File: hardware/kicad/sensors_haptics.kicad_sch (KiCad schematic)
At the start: 9 parts, among them J9 LRA motor, U10 VEML7700-TT, U11 DRV2605LDGSR

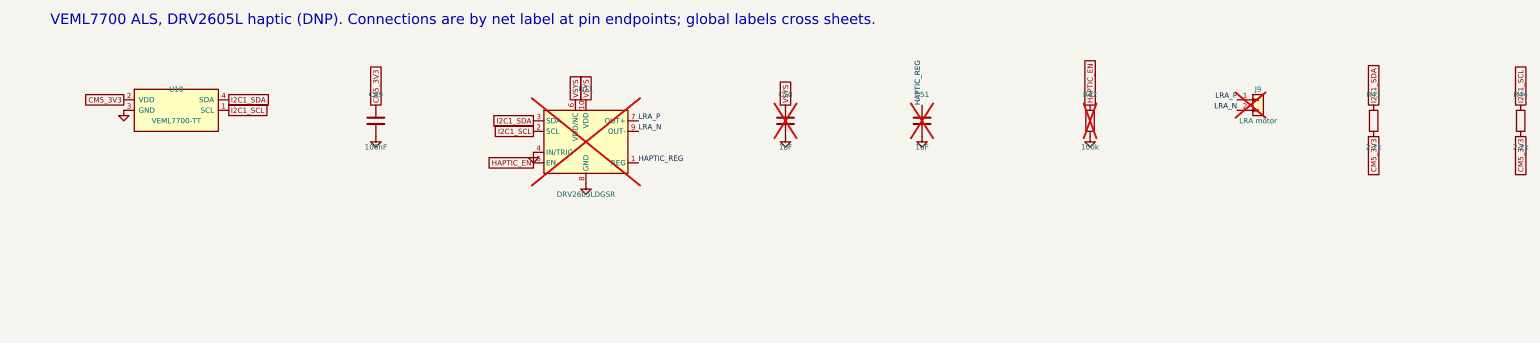
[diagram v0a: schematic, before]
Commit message: Sync KiCad schematic to netlist v3.2; add side_flex sheet
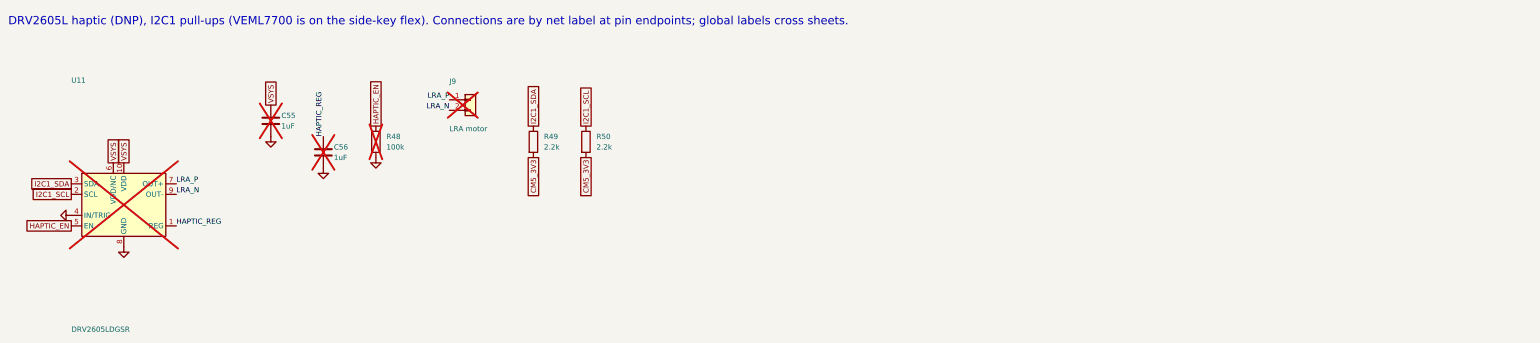
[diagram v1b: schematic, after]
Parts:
- removed C49: 100nF, Capacitor_SMD:C_0402_1005Metric, symbol Device:C
- removed C50, C51: 1uF, Capacitor_SMD:C_0402_1005Metric, symbol Device:C
- removed R42: 100k, Resistor_SMD:R_0402_1005Metric, symbol Device:R
- removed R43, R44: 2.2k, Resistor_SMD:R_0402_1005Metric, symbol Device:R
- removed U10: VEML7700-TT, symbol PocketMate:VEML7700
- added C55, C56: 1uF, Capacitor_SMD:C_0402_1005Metric, symbol Device:C
- added R48: 100k, Resistor_SMD:R_0402_1005Metric, symbol Device:R
- added R49, R50: 2.2k, Resistor_SMD:R_0402_1005Metric, symbol Device:R
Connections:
- net CM5_3V3: now also R49.2, R50.2
- net GND: now also C55.2, C56.2, R48.2
- net HAPTIC_EN: now also R48.1
- net HAPTIC_REG: now also C56.1
- net I2C1_SCL: now also R50.1
- net I2C1_SDA: now also R49.1
- net VSYS: now also C55.1
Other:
- note added: "DRV2605L haptic (DNP), I2C1 pull-ups (VEML7700 is on the side-key flex). Connections are by net label at pin endpoints; global labels cross sheets."
- note removed: "VEML7700 ALS, DRV2605L haptic (DNP). Connections are by net label at pin endpoints; global labels cross sheets."
- title: PocketMate - VEML7700 ALS, DRV2605L haptic (DNP) -> PocketMate - Sensors
